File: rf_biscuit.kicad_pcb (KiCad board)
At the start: 2 copper layers, 37 x 24 mm, 64 parts, among them P101 BNC, P102 BNC, U101 36103205_HF_Shield

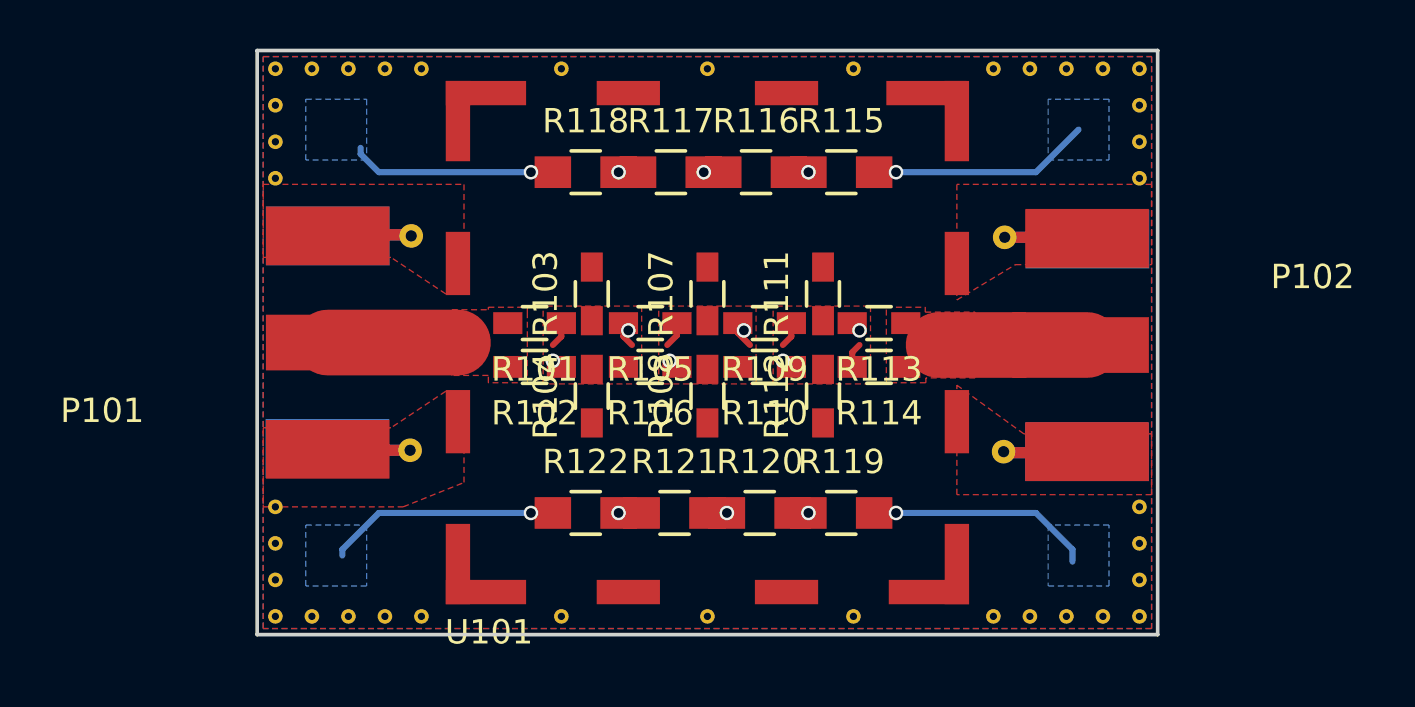
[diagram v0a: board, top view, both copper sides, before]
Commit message: Heavily modified and updated to KiCAD 6.0
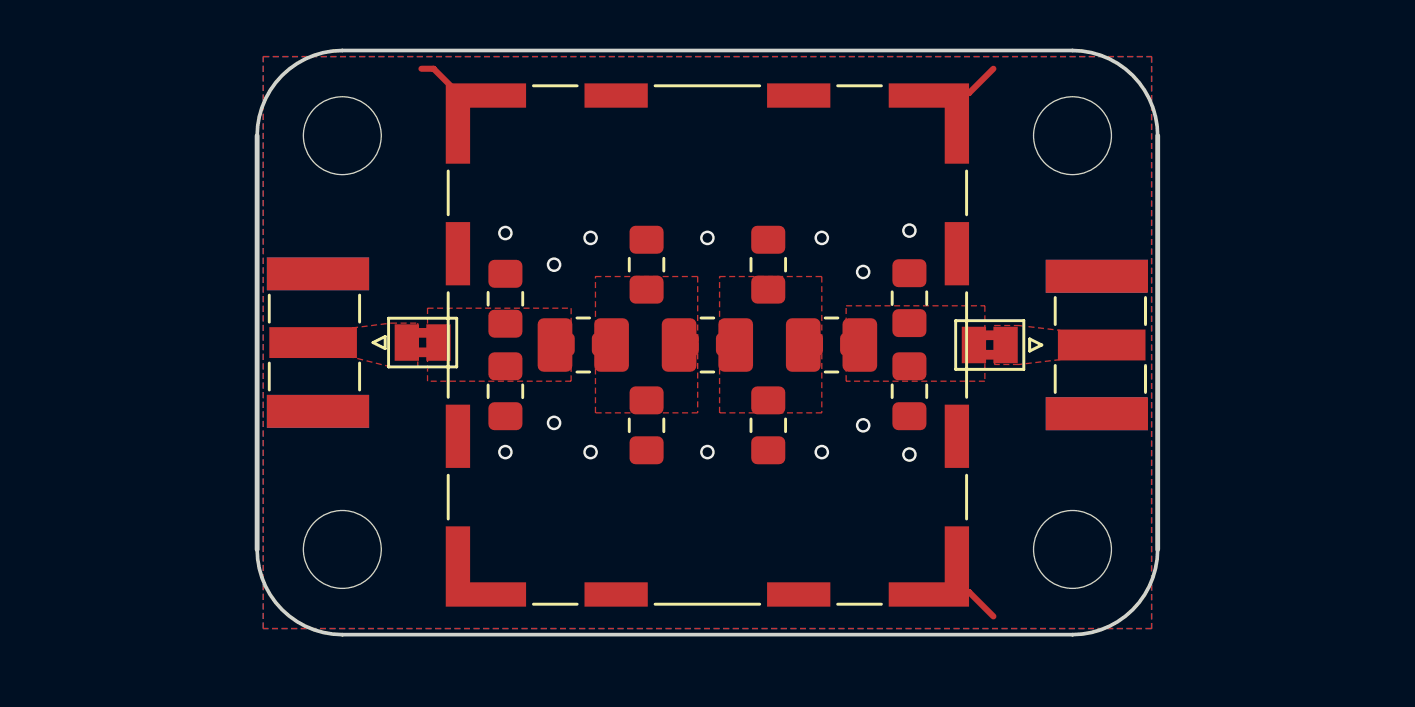
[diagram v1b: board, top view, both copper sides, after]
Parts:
- removed P101: BNC, Sockets_BNC:SMA_EDGE_CONNECTOR
- removed R101, R102, R106, R110, R114: R, Resistors_SMD:R_0603_HandSoldering
- removed R115, R116, R117, R118, R119, R120, R121, R122: R, Resistors_SMD:R_0805_HandSoldering
- removed REF** (x38): StichVIA, Sockets_BNC:StichVIA
- removed REF**: Symbol_OSHW-Logo_Mask, Sockets_BNC:Symbol_OSHW-Logo_Mask
- removed U101: 36103205_HF_Shield, Sockets_BNC:36103205-HF_Shield
- added H1: MountingHole, MountingHole:MountingHole_3.2mm_M3, F.Cu at (61.0, 100.5)
- added H2: MountingHole, MountingHole:MountingHole_3.2mm_M3, F.Cu at (61.0, 83.5)
- added H3: MountingHole, MountingHole:MountingHole_3.2mm_M3, F.Cu at (31.0, 100.5)
- added H4: MountingHole, MountingHole:MountingHole_3.2mm_M3, F.Cu at (31.0, 83.5)
- added J1: RFShield_OnePiece, RF_Shielding:Wuerth_36103205_20x20mm, F.Cu at (46.0, 92.1)
- added JP1: SolderJumper_2_Bridged, Jumper:SolderJumper-2_P1.3mm_Bridged2Bar_Pad1.0x1.5mm, F.Cu at (34.3, 92.0)
- added JP2: SolderJumper_2_Bridged, Jumper:SolderJumper-2_P1.3mm_Bridged2Bar_Pad1.0x1.5mm, F.Cu at (57.6, 92.1)
- added P1: BNC, Connector_Coaxial:SMA_Samtec_SMA-J-P-X-ST-EM1_EdgeMount, F.Cu at (30.0, 92.0)
- added R10: R, Inductor_SMD:L_0805_2012Metric_Pad1.15x1.40mm_HandSolder, F.Cu at (54.3, 94.0)
- added R11: R, Inductor_SMD:L_0805_2012Metric_Pad1.15x1.40mm_HandSolder, F.Cu at (54.3, 90.2)
- P2: renamed from P102; footprint Sockets_BNC:SMA_EDGE_CONNECTOR -> Connector_Coaxial:SMA_Samtec_SMA-J-P-X-ST-EM1_EdgeMount
- R1: renamed from R103; footprint Resistors_SMD:R_0603_HandSoldering -> Inductor_SMD:L_0805_2012Metric_Pad1.15x1.40mm_HandSolder
- R2: renamed from R104; footprint Resistors_SMD:R_0603_HandSoldering -> Inductor_SMD:L_0805_2012Metric_Pad1.15x1.40mm_HandSolder
- R3: renamed from R105; footprint Resistors_SMD:R_0603_HandSoldering -> hnch:L_1008_0805_0603_HandSolder_Combo
- R4: renamed from R107; footprint Resistors_SMD:R_0603_HandSoldering -> Inductor_SMD:L_0805_2012Metric_Pad1.15x1.40mm_HandSolder
- R5: renamed from R108; footprint Resistors_SMD:R_0603_HandSoldering -> Inductor_SMD:L_0805_2012Metric_Pad1.15x1.40mm_HandSolder
- R6: renamed from R109; footprint Resistors_SMD:R_0603_HandSoldering -> hnch:L_1008_0805_0603_HandSolder_Combo
- R7: renamed from R111; footprint Resistors_SMD:R_0603_HandSoldering -> Inductor_SMD:L_0805_2012Metric_Pad1.15x1.40mm_HandSolder
- R8: renamed from R112; footprint Resistors_SMD:R_0603_HandSoldering -> Inductor_SMD:L_0805_2012Metric_Pad1.15x1.40mm_HandSolder
- R9: renamed from R113; footprint Resistors_SMD:R_0603_HandSoldering -> hnch:L_1008_0805_0603_HandSolder_Combo
- moved R1 3.56 mm to (37.7, 90.2)
- moved R2 3.56 mm to (37.7, 94.0)
- moved R3 2.89 mm to (40.9, 92.1)
- moved R4 2.77 mm to (43.5, 88.8)
- moved R5 2.77 mm to (43.5, 95.4)
- moved R7 2.55 mm to (48.5, 88.8)
- moved R8 2.55 mm to (48.5, 95.4)
- moved R6 2.52 mm to (46.0, 92.1)
- moved R9 2.15 mm to (51.1, 92.1)
- moved P2 2.14 mm to (62.0, 92.1), turned to 90 degrees
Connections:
- P2 pad 1: Net-(P102-Pad1) -> Net-(JP2-Pad2)
- R9 pad 1: Net-(P102-Pad1) -> Net-(JP2-Pad1)
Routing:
- net GND: track 0.50 -> 11.2 mm, vias 0 -> 14
- net Net-(R122-Pad1): track 9.52 -> 0.00 mm, vias 1 -> 0
- net Net-(R119-Pad2): track 9.27 -> 0.00 mm, vias 1 -> 0
- net Net-(R115-Pad2): track 9.12 -> 0.00 mm, vias 1 -> 0
- net Net-(R118-Pad1): track 8.46 -> 0.00 mm, vias 1 -> 0
- net Net-(P102-Pad1): track 6.10 -> 0.00 mm
- net Net-(P101-Pad1): track 5.35 -> 0.00 mm
- net Net-(R3-Pad1): track 2.17 -> 0.00 mm, vias 2 -> 0
- net Net-(JP1-Pad2): track 2.09 -> 0.00 mm, vias 2 -> 0
- net Net-(R6-Pad1): track 2.07 -> 0.00 mm, vias 2 -> 0
- net Net-(R121-Pad1): track 0.95 -> 0.00 mm, vias 1 -> 0
- net Net-(R120-Pad1): track 0.80 -> 0.00 mm, vias 1 -> 0
- net Net-(R116-Pad1): track 0.80 -> 0.00 mm, vias 1 -> 0
- net Net-(R115-Pad1): track 0.80 -> 0.00 mm, vias 1 -> 0
- net Net-(R119-Pad1): track 0.65 -> 0.00 mm, vias 1 -> 0
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- added copper zone on F.Cu, net Net-(JP1-Pad1)
- added copper zone on F.Cu, net Net-(JP2-Pad1)
- added copper zone on F.Cu, net Net-(JP2-Pad2)
- removed copper zone on F.Cu, net Net-(P101-Pad1)
- removed copper zone on F.Cu, net Net-(P102-Pad1)
- removed copper zone on B.Cu, net Net-(R115-Pad2)
- removed copper zone on B.Cu, net Net-(R118-Pad1)
- removed copper zone on B.Cu, net Net-(R119-Pad2)
- removed copper zone on B.Cu, net Net-(R122-Pad1)
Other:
- outline, holes or cut-outs redrawn
- net class Default removed
- board text added: "CC BY-SA 3.0 (c) Otelo eGen, hnch DC4HP"
- board text added: "RF BISCUIT Rev. tbd"
- board text removed: "CC BY-SA 3.0 (c) Otelo eGen"
- board text removed: "RF BISCUIT Rev. A"
